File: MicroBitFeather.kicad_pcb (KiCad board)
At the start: 2 copper layers, 67.3 x 35.6 mm, 16 parts, among them J1 Feather_Long, J2 Barrel_Jack_MountingPin, J3 Feather_Short, J4 NeoPixels, J5 microbit_edge_connector, U1 74AHCT125, U2 MCP1702-3302E_TO92

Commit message: More tracks.
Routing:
- net /P6: track 0.00 -> 64.3 mm
- net /P12: track 0.00 -> 56.9 mm
- net /P7: track 0.00 -> 51.5 mm, vias 0 -> 1
- net /MISO: track 0.00 -> 32.1 mm
- net /MOSI: track 34.7 -> 34.1 mm
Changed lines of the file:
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@@
     (thickness 1.6)
     (drawings 12)
-    (tracks 196)
+    (tracks 255)
     (zones 0)
     (modules 16)
@@
   (segment (start 156.21 106.68) (end 156.21 110.49) (width 0.508) (layer F.Cu) (net 3))
   (segment (start 156.21 110.49) (end 157.48 111.76) (width 0.508) (layer F.Cu) (net 3))
+  (segment (start 129.119999 115.990001) (end 128.27 116.84) (width 0.508) (layer F.Cu) (net 4))
+  (segment (start 131.564002 113.545998) (end 129.119999 115.990001) (width 0.508) (layer F.Cu) (net 4))
+  (segment (start 142.994002 113.545998) (end 131.564002 113.545998) (width 0.508) (layer F.Cu) (net 4))
+  (segment (start 144.78 111.76) (end 142.994002 113.545998) (width 0.508) (layer F.Cu) (net 4))
   (segment (start 158.75 89.54) (end 156.21 89.54) (width 0.508) (layer F.Cu) (net 4))
   (segment (start 161.29 89.54) (end 158.75 89.54) (width 0.508) (layer F.Cu) (net 4))
@@
   (segment (start 168.872 97.79) (end 162.56 91.478) (width 0.508) (layer F.Cu) (net 4))
   (segment (start 162.56 91.478) (end 162.56 91.44) (width 0.508) (layer F.Cu) (net 4))
-  (segment (start 144.78 111.76) (end 141.004001 115.535999) (width 0.508) (layer F.Cu) (net 4))
-  (segment (start 141.004001 115.535999) (end 129.574001 115.535999) (width 0.508) (layer F.Cu) (net 4))
-  (segment (start 129.574001 115.535999) (end 129.119999 115.990001) (width 0.508) (layer F.Cu) (net 4))
-  (segment (start 129.119999 115.990001) (end 128.27 116.84) (width 0.508) (layer F.Cu) (net 4))
   (segment (start 148.59 101.6) (end 148.59 107.95) (width 0.508) (layer F.Cu) (net 4))
   (segment (start 148.59 107.95) (end 144.78 111.76) (width 0.508) (layer F.Cu) (net 4))
@@
   (segment (start 149.418999 90.289999) (end 150.380001 90.289999) (width 0.25) (layer B.Cu) (net 13))
   (segment (start 150.380001 90.289999) (end 151.13 89.54) (width 0.25) (layer B.Cu) (net 13))
-  (segment (start 153.67 116.84) (end 152.494999 115.664999) (width 0.25) (layer B.Cu) (net 14))
-  (segment (start 152.494999 115.664999) (end 150.237997 115.664999) (width 0.25) (layer B.Cu) (net 14))
-  (segment (start 150.237997 115.664999) (end 147.064999 112.492001) (width 0.25) (layer B.Cu) (net 14))
-  (segment (start 147.064999 112.492001) (end 147.064999 99.247082) (width 0.25) (layer B.Cu) (net 14))
-  (segment (start 147.064999 99.247082) (end 148.59 97.722081) (width 0.25) (layer B.Cu) (net 14))
-  (segment (start 148.59 97.722081) (end 148.59 96.52) (width 0.25) (layer B.Cu) (net 14))
+  (segment (start 148.59 97.342176) (end 148.59 96.52) (width 0.25) (layer B.Cu) (net 14))
+  (segment (start 146.164977 103.382801) (end 146.164977 99.767199) (width 0.25) (layer B.Cu) (net 14))
+  (segment (start 146.164977 99.767199) (end 148.59 97.342176) (width 0.25) (layer B.Cu) (net 14))
+  (segment (start 153.67 110.887823) (end 146.164977 103.382801) (width 0.25) (layer B.Cu) (net 14))
+  (segment (start 153.67 116.84) (end 153.67 110.887823) (width 0.25) (layer B.Cu) (net 14))
   (segment (start 148.59 96.52) (end 151.324999 93.785001) (width 0.25) (layer B.Cu) (net 14))
   (segment (start 151.324999 93.785001) (end 151.324999 90.923999) (width 0.25) (layer B.Cu) (net 14))
@@
   (segment (start 151.958999 90.289999) (end 152.920001 90.289999) (width 0.25) (layer B.Cu) (net 14))
   (segment (start 152.920001 90.289999) (end 153.67 89.54) (width 0.25) (layer B.Cu) (net 14))
+  (segment (start 146.614988 103.196401) (end 156.21 112.791412) (width 0.25) (layer B.Cu) (net 15))
+  (segment (start 152.044988 91.795012) (end 152.044988 93.86601) (width 0.25) (layer B.Cu) (net 15))
+  (segment (start 146.614988 99.953599) (end 146.614988 103.196401) (width 0.25) (layer B.Cu) (net 15))
+  (segment (start 148.595007 98.609989) (end 147.958598 98.609989) (width 0.25) (layer B.Cu) (net 15))
+  (segment (start 147.958598 98.609989) (end 146.614988 99.953599) (width 0.25) (layer B.Cu) (net 15))
+  (segment (start 149.765001 96.145997) (end 149.765001 97.439997) (width 0.25) (layer B.Cu) (net 15))
+  (segment (start 152.044988 93.86601) (end 149.765001 96.145997) (width 0.25) (layer B.Cu) (net 15))
+  (segment (start 152.4 91.44) (end 152.044988 91.795012) (width 0.25) (layer B.Cu) (net 15))
+  (segment (start 149.765001 97.439997) (end 148.595007 98.609989) (width 0.25) (layer B.Cu) (net 15))
+  (segment (start 156.21 112.791412) (end 156.21 115.637919) (width 0.25) (layer B.Cu) (net 15))
+  (segment (start 156.21 115.637919) (end 156.21 116.84) (width 0.25) (layer B.Cu) (net 15))
+  (segment (start 132.08 91.44) (end 131.330001 90.690001) (width 0.25) (layer B.Cu) (net 16))
+  (segment (start 131.330001 90.690001) (end 130.381003 90.690001) (width 0.25) (layer B.Cu) (net 16))
+  (segment (start 129.861002 90.17) (end 129.231002 90.17) (width 0.25) (layer B.Cu) (net 16))
+  (segment (start 130.381003 90.690001) (end 129.861002 90.17) (width 0.25) (layer B.Cu) (net 16))
+  (segment (start 129.231002 90.17) (end 128.27 91.131002) (width 0.25) (layer B.Cu) (net 16))
+  (segment (start 128.27 91.131002) (end 128.27 91.761002) (width 0.25) (layer B.Cu) (net 16))
+  (segment (start 128.27 91.761002) (end 127.094999 92.936003) (width 0.25) (layer B.Cu) (net 16))
+  (segment (start 127.094999 92.936003) (end 127.094999 117.404001) (width 0.25) (layer B.Cu) (net 16))
+  (segment (start 127.094999 117.404001) (end 128.156009 118.465011) (width 0.25) (layer B.Cu) (net 16))
+  (segment (start 128.156009 118.465011) (end 157.124989 118.465011) (width 0.25) (layer B.Cu) (net 16))
+  (segment (start 157.124989 118.465011) (end 157.900001 117.689999) (width 0.25) (layer B.Cu) (net 16))
+  (segment (start 157.900001 117.689999) (end 158.75 116.84) (width 0.25) (layer B.Cu) (net 16))
+  (segment (start 137.16 114.3) (end 134.714999 111.854999) (width 0.25) (layer B.Cu) (net 17))
+  (segment (start 134.714999 111.854999) (end 134.714999 93.126001) (width 0.25) (layer B.Cu) (net 17))
+  (segment (start 134.714999 93.126001) (end 133.35 91.761002) (width 0.25) (layer B.Cu) (net 17))
+  (segment (start 133.35 91.761002) (end 133.35 90.60066) (width 0.25) (layer B.Cu) (net 17))
+  (segment (start 133.35 90.60066) (end 133.35 89.54) (width 0.25) (layer B.Cu) (net 17))
+  (segment (start 161.29 116.84) (end 158.75 114.3) (width 0.25) (layer F.Cu) (net 17))
+  (segment (start 158.75 114.3) (end 137.16 114.3) (width 0.25) (layer F.Cu) (net 17))
+  (via (at 137.16 114.3) (size 0.6) (drill 0.4) (layers F.Cu B.Cu) (net 17))
+  (segment (start 153.67 87.961002) (end 153.67 87.318998) (width 0.25) (layer B.Cu) (net 18))
+  (segment (start 148.073999 88.464999) (end 147.638998 88.9) (width 0.25) (layer B.Cu) (net 18))
+  (segment (start 153.67 87.318998) (end 152.916001 86.564999) (width 0.25) (layer B.Cu) (net 18))
+  (segment (start 152.916001 86.564999) (end 151.883999 86.564999) (width 0.25) (layer B.Cu) (net 18))
+  (segment (start 145.533999 88.464999) (end 144.78 89.218998) (width 0.25) (layer B.Cu) (net 18))
+  (segment (start 151.883999 86.564999) (end 150.935001 87.513997) (width 0.25) (layer B.Cu) (net 18))
+  (segment (start 150.935001 88.156001) (end 150.191002 88.9) (width 0.25) (layer B.Cu) (net 18))
+  (segment (start 149.106001 88.464999) (end 148.073999 88.464999) (width 0.25) (layer B.Cu) (net 18))
+  (segment (start 146.566001 88.464999) (end 145.533999 88.464999) (width 0.25) (layer B.Cu) (net 18))
+  (segment (start 144.78 90.37934) (end 144.78 91.44) (width 0.25) (layer B.Cu) (net 18))
+  (segment (start 150.935001 87.513997) (end 150.935001 88.156001) (width 0.25) (layer B.Cu) (net 18))
+  (segment (start 150.191002 88.9) (end 149.541002 88.9) (width 0.25) (layer B.Cu) (net 18))
+  (segment (start 149.541002 88.9) (end 149.106001 88.464999) (width 0.25) (layer B.Cu) (net 18))
+  (segment (start 147.638998 88.9) (end 147.001002 88.9) (width 0.25) (layer B.Cu) (net 18))
+  (segment (start 147.001002 88.9) (end 146.566001 88.464999) (width 0.25) (layer B.Cu) (net 18))
+  (segment (start 144.78 89.218998) (end 144.78 90.37934) (width 0.25) (layer B.Cu) (net 18))
+  (segment (start 154.94 89.861002) (end 154.94 89.231002) (width 0.25) (layer B.Cu) (net 18))
+  (segment (start 152.494999 92.936003) (end 153.67 91.761002) (width 0.25) (layer B.Cu) (net 18))
+  (segment (start 150.329002 99.06) (end 152.494999 96.894003) (width 0.25) (layer B.Cu) (net 18))
+  (segment (start 148.144998 99.06) (end 150.329002 99.06) (width 0.25) (layer B.Cu) (net 18))
+  (segment (start 152.494999 96.894003) (end 152.494999 92.936003) (width 0.25) (layer B.Cu) (net 18))
+  (segment (start 153.67 91.761002) (end 153.67 91.131002) (width 0.25) (layer B.Cu) (net 18))
+  (segment (start 153.67 91.131002) (end 154.94 89.861002) (width 0.25) (layer B.Cu) (net 18))
+  (segment (start 154.94 89.231002) (end 153.67 87.961002) (width 0.25) (layer B.Cu) (net 18))
+  (segment (start 163.83 116.84) (end 159.875001 112.885001) (width 0.25) (layer B.Cu) (net 18))
+  (segment (start 159.875001 112.885001) (end 156.939999 112.885001) (width 0.25) (layer B.Cu) (net 18))
+  (segment (start 156.939999 112.885001) (end 147.064999 103.010001) (width 0.25) (layer B.Cu) (net 18))
+  (segment (start 147.064999 103.010001) (end 147.064999 100.139999) (width 0.25) (layer B.Cu) (net 18))
+  (segment (start 147.064999 100.139999) (end 148.144998 99.06) (width 0.25) (layer B.Cu) (net 18))
   (segment (start 137.16 101.6) (end 137.16 97.79) (width 0.25) (layer F.Cu) (net 19))
   (segment (start 137.16 97.79) (end 138.43 96.52) (width 0.25) (layer F.Cu) (net 19))

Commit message: Finish tracks.
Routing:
- net Net-(J4-Pad2): track 0.00 -> 40.6 mm, vias 0 -> 4
- net Net-(R2-Pad1): track 0.00 -> 23.4 mm
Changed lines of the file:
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@@
     (thickness 1.6)
     (drawings 12)
-    (tracks 255)
+    (tracks 273)
     (zones 0)
     (modules 16)
@@
   (segment (start 163.83 96.52) (end 163.83 92.71) (width 0.25) (layer B.Cu) (net 26))
   (segment (start 163.83 92.71) (end 165.1 91.44) (width 0.25) (layer B.Cu) (net 26))
+  (segment (start 157.48 99.06) (end 158.02 99.6) (width 0.25) (layer F.Cu) (net 27))
+  (segment (start 158.02 99.6) (end 178.435 99.6) (width 0.25) (layer F.Cu) (net 27))
+  (segment (start 151.13 104.14) (end 152.4 104.14) (width 0.25) (layer B.Cu) (net 27))
+  (segment (start 152.4 104.14) (end 157.48 99.06) (width 0.25) (layer B.Cu) (net 27))
+  (via (at 157.48 99.06) (size 0.6) (drill 0.4) (layers F.Cu B.Cu) (net 27))
+  (segment (start 148.59 109.22) (end 151.13 106.68) (width 0.25) (layer F.Cu) (net 27))
+  (segment (start 151.13 106.68) (end 151.13 104.14) (width 0.25) (layer F.Cu) (net 27))
+  (via (at 151.13 104.14) (size 0.6) (drill 0.4) (layers F.Cu B.Cu) (net 27))
+  (segment (start 147.32 107.95) (end 148.59 109.22) (width 0.25) (layer B.Cu) (net 27))
+  (via (at 148.59 109.22) (size 0.6) (drill 0.4) (layers F.Cu B.Cu) (net 27))
+  (segment (start 144.78 106.68) (end 146.05 106.68) (width 0.25) (layer F.Cu) (net 27))
+  (segment (start 146.05 106.68) (end 147.32 107.95) (width 0.25) (layer F.Cu) (net 27))
+  (via (at 147.32 107.95) (size 0.6) (drill 0.4) (layers F.Cu B.Cu) (net 27))
+  (segment (start 120.65 107.075002) (end 120.65 102.87) (width 0.25) (layer F.Cu) (net 68))
+  (segment (start 120.65 102.87) (end 121.92 101.6) (width 0.25) (layer F.Cu) (net 68))
+  (segment (start 137.16 106.68) (end 135.89 107.95) (width 0.25) (layer F.Cu) (net 68))
+  (segment (start 135.89 107.95) (end 121.524998 107.95) (width 0.25) (layer F.Cu) (net 68))
+  (segment (start 121.524998 107.95) (end 120.65 107.075002) (width 0.25) (layer F.Cu) (net 68))
   (zone (net 1) (net_name +5V) (layer F.Cu) (hatch edge 0.508)
     (connect_pads (clearance 0.3048))

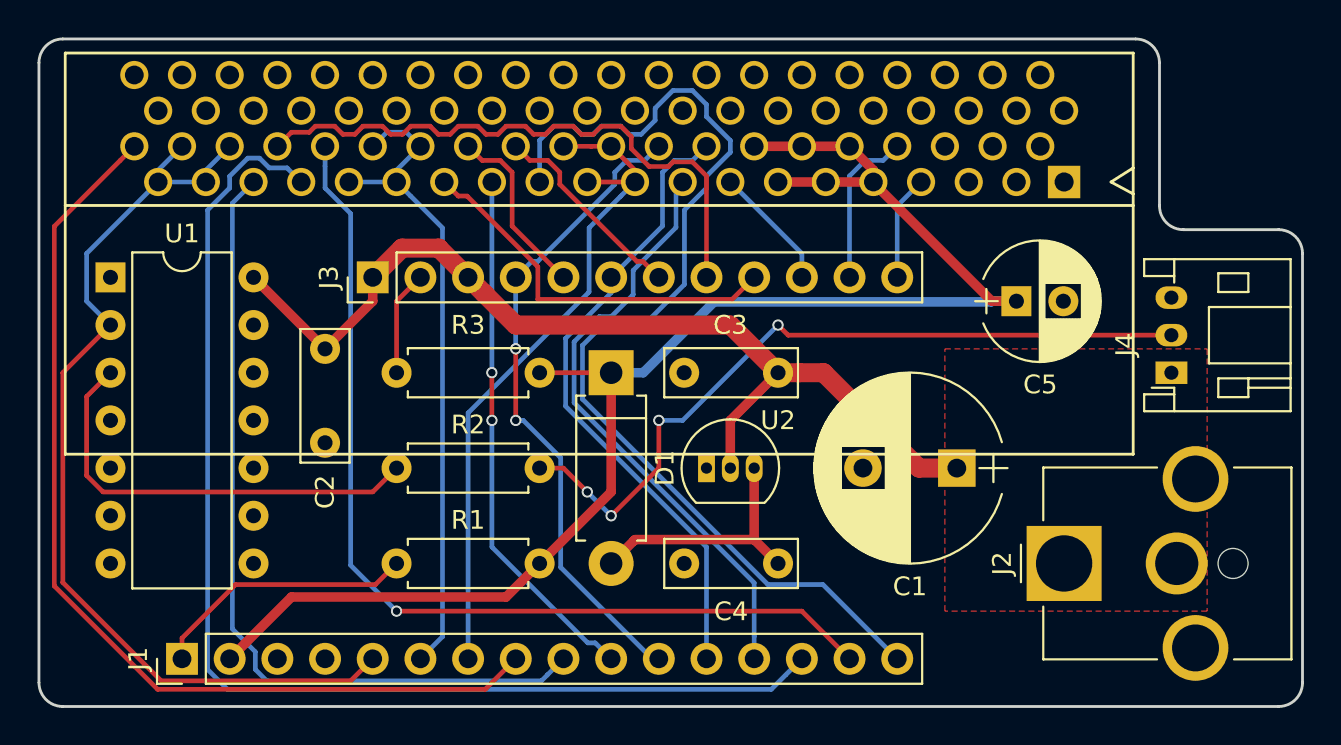
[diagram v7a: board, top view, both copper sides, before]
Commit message: Fill GND zones.
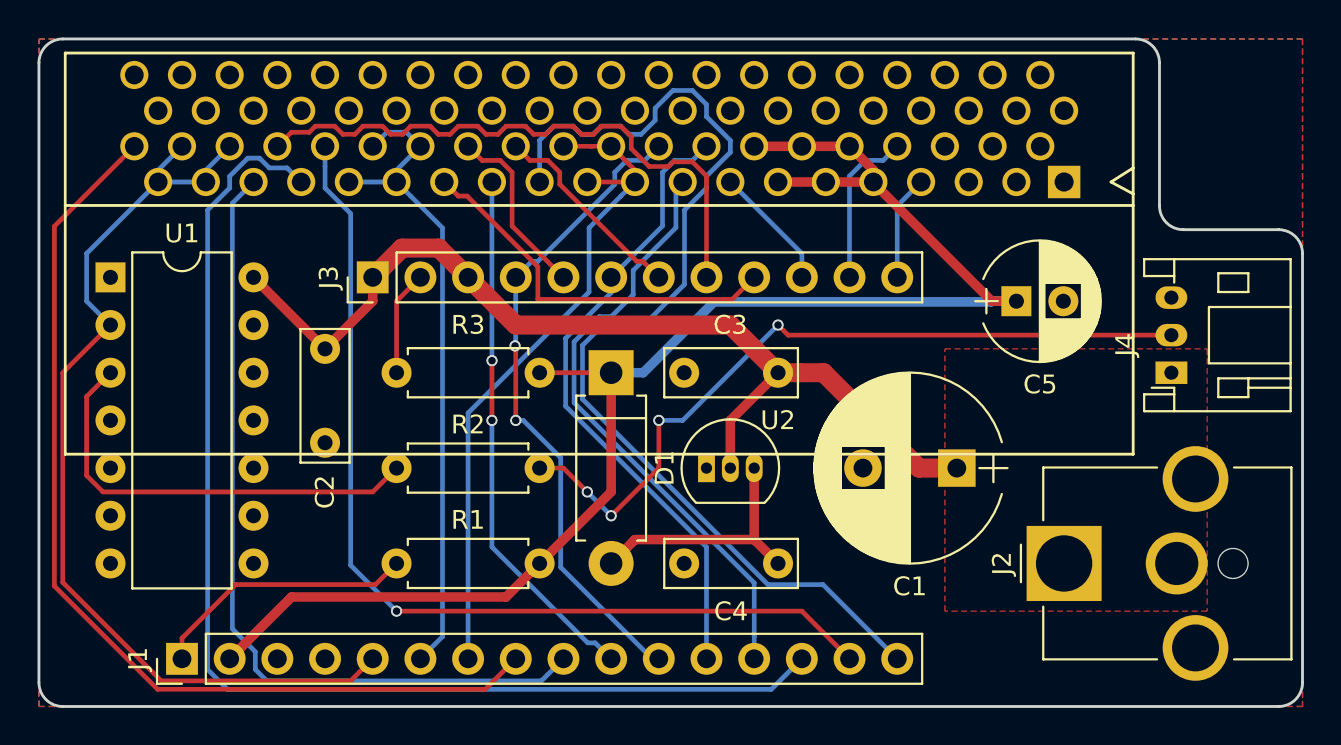
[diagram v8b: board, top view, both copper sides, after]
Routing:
- added copper zone on B.Cu, net GND
- added copper zone on F.Cu, net GND
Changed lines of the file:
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@@
   (general
     (links 79)
-    (no_connects 50)
+    (no_connects 3)
     (area 118.034999 83.744999 185.495001 119.455001)
     (thickness 1.6)
@@
     (pad_to_mask_clearance 0)
     (aux_axis_origin 0 0)
-    (visible_elements FFFEE77F)
+    (visible_elements FFFEF77F)
     (pcbplotparams
       (layerselection 0x00030_80000001)
@@
   (segment (start 144.874999 118.015001) (end 145.200001 117.689999) (width 0.25) (layer B.Cu) (net 11))
   (segment (start 145.200001 117.689999) (end 146.05 116.84) (width 0.25) (layer B.Cu) (net 11))
+  (segment (start 142.24 100.953453) (end 142.243819 100.957272) (width 0.25) (layer B.Cu) (net 12))
+  (segment (start 142.24 91.44) (end 142.24 100.953453) (width 0.25) (layer B.Cu) (net 12))
+  (segment (start 142.24 100.961091) (end 142.243819 100.957272) (width 0.25) (layer F.Cu) (net 12))
+  (segment (start 142.24 104.14) (end 142.24 100.961091) (width 0.25) (layer F.Cu) (net 12))
+  (via (at 142.243819 100.957272) (size 0.6) (drill 0.4) (layers F.Cu B.Cu) (net 12))
   (segment (start 142.24 104.14) (end 142.24 110.885002) (width 0.25) (layer B.Cu) (net 12))
   (segment (start 142.24 110.885002) (end 147.344999 115.990001) (width 0.25) (layer B.Cu) (net 12))
   (segment (start 147.344999 115.990001) (end 147.740001 115.990001) (width 0.25) (layer B.Cu) (net 12))
   (segment (start 147.740001 115.990001) (end 148.59 116.84) (width 0.25) (layer B.Cu) (net 12))
-  (segment (start 142.235557 101.595557) (end 142.235557 104.135557) (width 0.25) (layer F.Cu) (net 12))
-  (segment (start 142.235557 104.135557) (end 142.24 104.14) (width 0.25) (layer F.Cu) (net 12))
   (via (at 142.24 104.14) (size 0.6) (drill 0.4) (layers F.Cu B.Cu) (net 12))
-  (segment (start 142.24 91.44) (end 142.24 101.591114) (width 0.25) (layer B.Cu) (net 12))
-  (segment (start 142.24 101.591114) (end 142.235557 101.595557) (width 0.25) (layer B.Cu) (net 12))
-  (via (at 142.235557 101.595557) (size 0.6) (drill 0.4) (layers F.Cu B.Cu) (net 12))
-  (segment (start 143.505557 100.325557) (end 143.505557 96.524443) (width 0.25) (layer B.Cu) (net 13))
-  (segment (start 143.505557 96.524443) (end 143.51 96.52) (width 0.25) (layer B.Cu) (net 13))
-  (segment (start 143.51 104.14) (end 143.51 100.33) (width 0.25) (layer F.Cu) (net 13))
-  (segment (start 143.51 100.33) (end 143.505557 100.325557) (width 0.25) (layer F.Cu) (net 13))
-  (via (at 143.505557 100.325557) (size 0.6) (drill 0.4) (layers F.Cu B.Cu) (net 13))
+  (segment (start 143.51 100.210597) (end 143.471815 100.172412) (width 0.25) (layer F.Cu) (net 13))
+  (segment (start 143.51 104.14) (end 143.51 100.210597) (width 0.25) (layer F.Cu) (net 13))
+  (segment (start 143.51 96.52) (end 143.51 100.134227) (width 0.25) (layer B.Cu) (net 13))
+  (segment (start 143.51 100.134227) (end 143.471815 100.172412) (width 0.25) (layer B.Cu) (net 13))
+  (via (at 143.471815 100.172412) (size 0.6) (drill 0.4) (layers F.Cu B.Cu) (net 13))
   (segment (start 151.13 116.84) (end 150.776588 116.84) (width 0.25) (layer B.Cu) (net 13))
   (segment (start 150.776588 116.84) (end 145.905001 111.968413) (width 0.25) (layer B.Cu) (net 13))
@@
   (segment (start 121.524998 107.95) (end 120.65 107.075002) (width 0.25) (layer F.Cu) (net 68))
   (zone (net 1) (net_name +5V) (layer F.Cu) (hatch edge 0.508)
+    (priority 1)
     (connect_pads (clearance 0.3048))
     (min_thickness 0.254)
-    (fill (arc_segments 16) (thermal_gap 0.508) (thermal_bridge_width 0.508))
+    (fill yes (arc_segments 16) (thermal_gap 0.508) (thermal_bridge_width 0.508))
     (polygon
       (pts
@@
       )
     )
+  )
+  (zone (net 2) (net_name GND) (layer B.Cu) (hatch edge 0.508)
+    (connect_pads (clearance 0.3048))
+    (min_thickness 0.254)
+    (fill yes (arc_segments 16) (thermal_gap 0.508) (thermal_bridge_width 0.508))
+    (polygon
+      (pts
+        (xy 185.42 119.38) (xy 118.11 119.38) (xy 118.11 83.82) (xy 185.42 83.82)
+      )
+    )
+  )
+  (zone (net 2) (net_name GND) (layer F.Cu) (hatch edge 0.508)
+    (connect_pads (clearance 0.3048))
+    (min_thickness 0.254)
+    (fill yes (arc_segments 16) (thermal_gap 0.508) (thermal_bridge_width 0.508))
+    (polygon
+      (pts
+        (xy 185.42 119.38) (xy 118.11 119.38) (xy 118.11 83.82) (xy 185.42 83.82)
+      )
+    )
